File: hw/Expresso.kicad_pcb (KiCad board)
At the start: 4 copper layers, 76.2 x 59.4 mm, 93 parts, among them J1 USB_C_Receptacle_USB2.0_16P, J11 Exp Connector, J13 Exp Connector, J3 Midi Out, J5 Debug, J7 Exp Connector, J9 Exp Connector, SW1 Reset, SW2 Boot0, U1 XC6206P332MR, U10 NE5532, U2 XC6206P332MR, U3 STM32G431CBT6, U4 SRV05-4, U5 74HC14, U7 NE5532, U8 NE5532, U9 NE5532, Y1 16 MHz

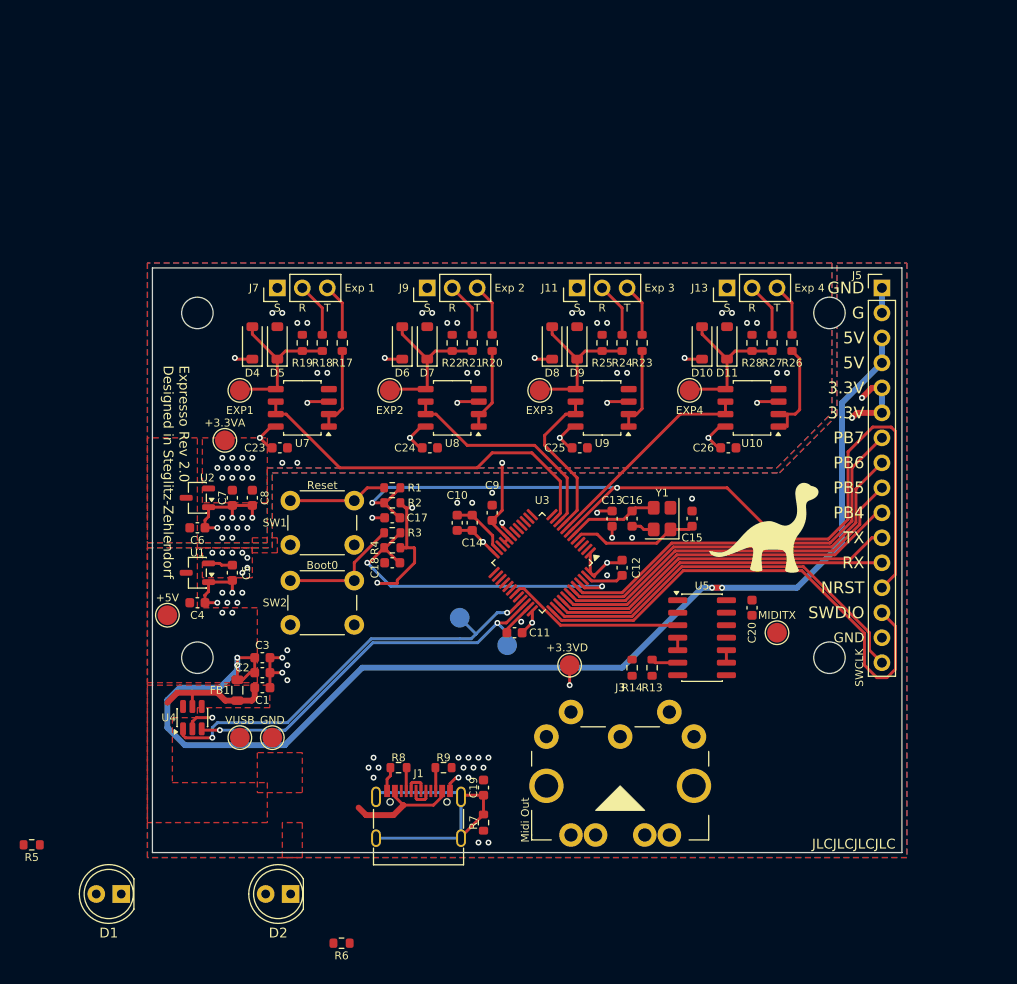
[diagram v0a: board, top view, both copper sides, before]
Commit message: added new pcb design, ERC errors not fixed yet
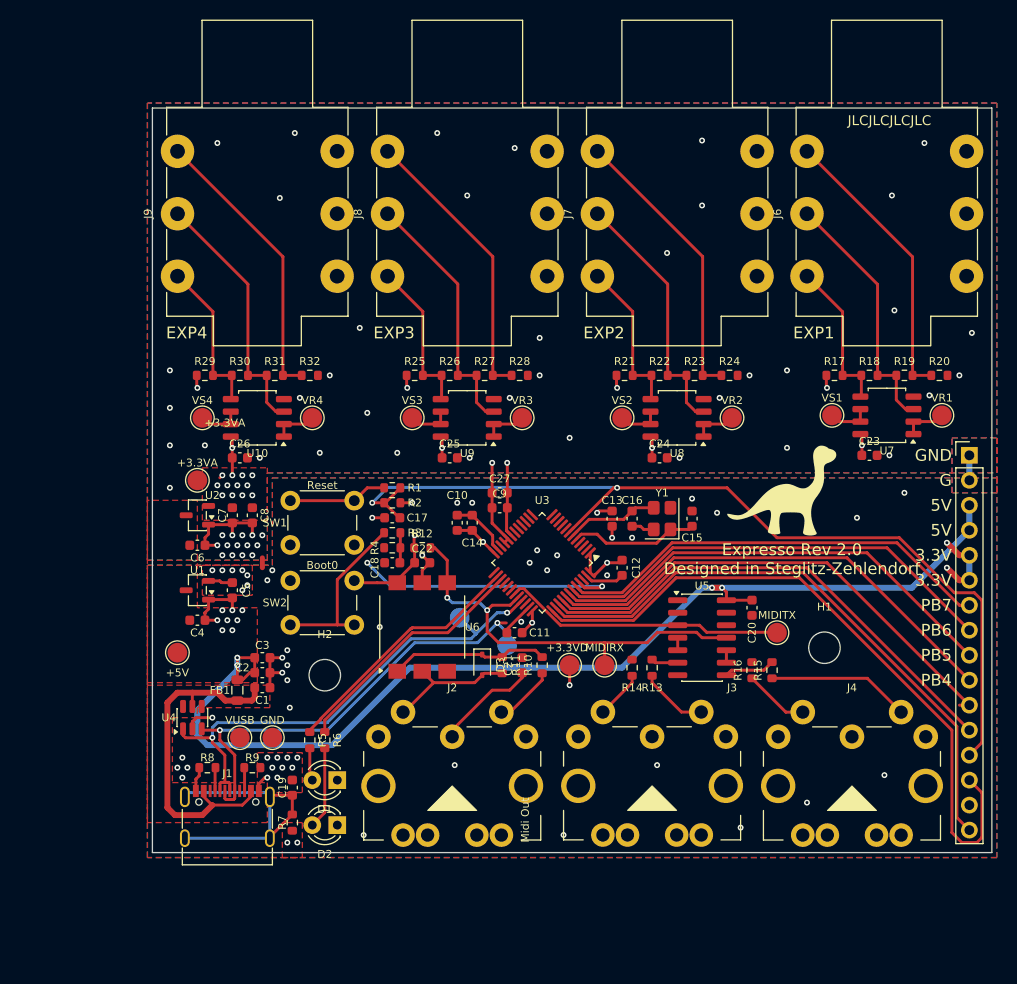
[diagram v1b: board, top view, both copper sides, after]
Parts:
- removed D10, D11, D4, D5, D6, D7, D8, D9: B5819W SL, Diode_SMD:D_SOD-123
- removed H3, H4: MountingHole, MountingHole:MountingHole_3.2mm_M3
- removed J11, J13: Exp Connector, Connector_PinHeader_2.54mm:PinHeader_1x03_P2.54mm_Vertical
- added C21: 100n, Capacitor_SMD:C_0603_1608Metric, F.Cu at (161.0, 126.2)
- added C22: 100n, Capacitor_SMD:C_0603_1608Metric, F.Cu at (150.9, 115.8)
- added C27: 1u, Capacitor_SMD:C_0603_1608Metric, F.Cu at (158.8, 108.7)
- added D3: 1N4148WS, Diode_SMD:D_SOD-323, F.Cu at (157.0, 126.2)
- added J2: Midi In, DIN5_MIDI_MultiGround:DIN5_MIDI_MultiGround, F.Cu at (153.9, 133.5)
- added J4: Midi Thru, DIN5_MIDI_MultiGround:DIN5_MIDI_MultiGround, F.Cu at (194.6, 133.5)
- added J6: Exp, Connector_Audio:Jack_6.35mm_Neutrik_NMJ6HFD4_Horizontal, F.Cu at (190.0, 86.7)
- added J8: Exp, Connector_Audio:Jack_6.35mm_Neutrik_NMJ6HFD4_Horizontal, F.Cu at (147.3, 86.7)
- added NT1: GND_GNDA, NetTie:NetTie-2_SMD_Pad0.5mm, F.Cu at (134.6, 115.8)
- added R10: 220, Resistor_SMD:R_0603_1608Metric, F.Cu at (163.1, 126.2)
- added R11: 1k, Resistor_SMD:R_0603_1608Metric, F.Cu at (159.0, 126.2)
- added R12: 1k, Resistor_SMD:R_0603_1608Metric, F.Cu at (150.9, 114.3)
- added R15: 220, Resistor_SMD:R_0603_1608Metric, F.Cu at (186.4, 126.7)
- added R16: 220, Resistor_SMD:R_0603_1608Metric, F.Cu at (184.4, 126.7)
- added R29: 10k, Resistor_SMD:R_0603_1608Metric, F.Cu at (128.8, 96.8)
- added R30: 100k, Resistor_SMD:R_0603_1608Metric, F.Cu at (132.3, 96.8)
- added R31: 100k, Resistor_SMD:R_0603_1608Metric, F.Cu at (135.9, 96.8)
- added R32: 10k, Resistor_SMD:R_0603_1608Metric, F.Cu at (139.4, 96.8)
- added TP11: VS, TestPoint:TestPoint_Pad_D2.0mm, F.Cu at (192.5, 100.8)
- added TP13: VS, TestPoint:TestPoint_Pad_D2.0mm, F.Cu at (171.2, 101.1)
- added TP15: VS, TestPoint:TestPoint_Pad_D2.0mm, F.Cu at (149.9, 101.1)
- added TP17: VS, TestPoint:TestPoint_Pad_D2.0mm, F.Cu at (128.5, 101.1)
- added TP8: MIDI_RX, TestPoint:TestPoint_Pad_D2.0mm, F.Cu at (169.4, 126.2)
- added U6: H11L1, SOP-6-2.54mm:SOP-6_6.35x8.51mm_P02.54mm, F.Cu at (150.9, 122.4)
- D1, D2: footprint LED_THT:LED_D5.0mm -> LED_THT:LED_D3.0mm
- J7, J9: value Exp Connector -> Exp; footprint Connector_PinHeader_2.54mm:PinHeader_1x03_P2.54mm_Vertical -> Connector_Audio:Jack_6.35mm_Neutrik_NMJ6HFD4_Horizontal
- R17, R20, R21, R24: value 1k -> 10k
- R18, R23, R26, R27: value 1k -> 100k
- R19, R22: value 2M -> 100k
- R25, R28: value 2M -> 10k
- TP10: renamed from TP8; value EXP -> VR
- TP12: renamed from TP9; value EXP -> VR
- TP14: renamed from TP10; value EXP -> VR
- TP16: renamed from TP11; value EXP -> VR
- moved H1 72.3 mm to (191.8, 124.5)
- moved TP10 71.4 mm to (203.7, 100.8)
- moved H2 63.2 mm to (141.0, 127.3)
- moved R19 61.3 mm to (199.9, 96.8), turned to 0 degrees
- moved C23 59.9 mm to (196.3, 104.9)
- moved U7 59.4 mm to (198.1, 100.8)
- moved R18 55.7 mm to (196.3, 96.8), turned to 0 degrees
- moved U10 50.3 mm to (134.1, 101.1)
- moved R17 50.1 mm to (192.8, 96.8), turned to 0 degrees
- moved C26 49.7 mm to (132.3, 105.2)
- moved R20 45.6 mm to (203.5, 96.8), turned to 0 degrees
- moved TP16 38.5 mm to (139.7, 101.1)
- moved R26 35.0 mm to (153.7, 96.8), turned to 0 degrees
- moved TP12 34.9 mm to (182.4, 101.1)
- moved J7 32.6 mm to (168.7, 86.7)
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- renumbered TP13 to TP6, TP12 to TP7, TP7 to TP9
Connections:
- C23 pad 2: GND -> GNDA
- C24 pad 2: GND -> GNDA
- C25 pad 2: GND -> GNDA
- C26 pad 2: GND -> GNDA
- C6 pad 2: GND -> GNDA
- C7 pad 2: GND -> GNDA
- C8 pad 2: GND -> GNDA
- C9 pad 2: GND -> GNDA
- R17 pad 1: Net-(J7-Pin_3) -> +3.3VA
- R17 pad 2: /Expression Inputs/Expression Input 1/EXP_REF -> /Expression Inputs/Expression Input 1/EXP_T
- R18 pad 1: Net-(J7-Pin_2) -> /Expression Inputs/Expression Input 1/EXP_T
- R18 pad 2: /Expression Inputs/Expression Input 1/EXP_SENSE -> /Expression Inputs/Expression Input 1/EXP_R
- R19 pad 1: /Expression Inputs/Expression Input 1/EXP_SENSE -> /Expression Inputs/Expression Input 1/EXP_R
- R19 pad 2: GND -> /Expression Inputs/Expression Input 1/EXP_S
- R20 pad 1: Net-(J9-Pin_3) -> /Expression Inputs/Expression Input 1/EXP_S
- R20 pad 2: /Expression Inputs/Expression Input 2/EXP_REF -> GNDA
- R21 pad 1: Net-(J9-Pin_2) -> +3.3VA
- R21 pad 2: /Expression Inputs/Expression Input 2/EXP_SENSE -> /Expression Inputs/Expression Input 2/EXP_T
- R22 pad 1: /Expression Inputs/Expression Input 2/EXP_SENSE -> /Expression Inputs/Expression Input 2/EXP_T
- R22 pad 2: GND -> /Expression Inputs/Expression Input 2/EXP_R
- R23 pad 1: Net-(J11-Pin_3) -> /Expression Inputs/Expression Input 2/EXP_R
- R23 pad 2: /Expression Inputs/Expression Input 3/EXP_REF -> /Expression Inputs/Expression Input 2/EXP_S
- R24 pad 1: Net-(J11-Pin_2) -> /Expression Inputs/Expression Input 2/EXP_S
- R24 pad 2: /Expression Inputs/Expression Input 3/EXP_SENSE -> GNDA
- R25 pad 1: /Expression Inputs/Expression Input 3/EXP_SENSE -> +3.3VA
- R25 pad 2: GND -> /Expression Inputs/Expression Input 3/EXP_T
- R26 pad 1: Net-(J13-Pin_3) -> /Expression Inputs/Expression Input 3/EXP_T
- R26 pad 2: /Expression Inputs/Expression Input 4/EXP_REF -> /Expression Inputs/Expression Input 3/EXP_R
- R27 pad 1: Net-(J13-Pin_2) -> /Expression Inputs/Expression Input 3/EXP_R
- R27 pad 2: /Expression Inputs/Expression Input 4/EXP_SENSE -> /Expression Inputs/Expression Input 3/EXP_S
- R28 pad 1: /Expression Inputs/Expression Input 4/EXP_SENSE -> /Expression Inputs/Expression Input 3/EXP_S
- R28 pad 2: GND -> GNDA
- R4 pad 1: STM_BOOT0 -> GND
- R4 pad 2: +3.3V -> STM_BOOT0
- SW2 pad 1: GND -> Net-(R3-Pad1)
- SW2 pad 2: Net-(R3-Pad1) -> +3.3V
- TP10 pad 1: /Expression Inputs/Expression Input 1/EXP_SENSE -> /Expression Inputs/Expression Input 1/VR
- TP12 pad 1: /Expression Inputs/Expression Input 2/EXP_SENSE -> /Expression Inputs/Expression Input 2/VR
- TP14 pad 1: /Expression Inputs/Expression Input 3/EXP_SENSE -> /Expression Inputs/Expression Input 3/VR
- TP16 pad 1: /Expression Inputs/Expression Input 4/EXP_SENSE -> /Expression Inputs/Expression Input 4/VR
- U10 pad 1: /Expression Inputs/Expression Input 4/EXP_REF -> /Expression Inputs/Expression Input 4/VR
- U10 pad 2: /Expression Inputs/Expression Input 4/EXP_REF -> /Expression Inputs/Expression Input 4/VR
- U10 pad 3: +3.3VA -> /Expression Inputs/Expression Input 4/EXP_R
- U10 pad 4: GND -> GNDA
- U10 pad 5: /Expression Inputs/Expression Input 4/EXP_SENSE -> /Expression Inputs/Expression Input 4/EXP_T
- U10 pad 6: STM_ADC1_IN1 -> /Expression Inputs/Expression Input 4/VS
- U10 pad 7: STM_ADC1_IN1 -> /Expression Inputs/Expression Input 4/VS
- U2 pad 1: GND -> GNDA
- U3 pad 19: GND -> GNDA
- U3 pad 32: unconnected-(U3-PA10-Pad32) -> STM_USART1_RX
- U5 pad 1: GND -> (no net)
- U5 pad 10: unconnected-(U5-Pad10) -> Net-(U5-Pad10)
- U5 pad 11: GND -> STM_USART1_RX
- U5 pad 12: unconnected-(U5-Pad12) -> (no net)
- U5 pad 13: GND -> (no net)
- U5 pad 2: unconnected-(U5-Pad2) -> (no net)
- U5 pad 8: unconnected-(U5-Pad8) -> Net-(R15-Pad2)
- U5 pad 9: GND -> Net-(U5-Pad10)
- U7 pad 1: /Expression Inputs/Expression Input 1/EXP_REF -> /Expression Inputs/Expression Input 1/VR
- U7 pad 2: /Expression Inputs/Expression Input 1/EXP_REF -> /Expression Inputs/Expression Input 1/VR
- U7 pad 3: +3.3VA -> /Expression Inputs/Expression Input 1/EXP_R
- U7 pad 4: GND -> GNDA
- U7 pad 5: /Expression Inputs/Expression Input 1/EXP_SENSE -> /Expression Inputs/Expression Input 1/EXP_T
- U7 pad 6: STM_ADC1_IN4 -> /Expression Inputs/Expression Input 1/VS
- U7 pad 7: STM_ADC1_IN4 -> /Expression Inputs/Expression Input 1/VS
- U8 pad 1: /Expression Inputs/Expression Input 2/EXP_REF -> /Expression Inputs/Expression Input 2/VR
- U8 pad 2: /Expression Inputs/Expression Input 2/EXP_REF -> /Expression Inputs/Expression Input 2/VR
- U8 pad 3: +3.3VA -> /Expression Inputs/Expression Input 2/EXP_R
- U8 pad 4: GND -> GNDA
- U8 pad 5: /Expression Inputs/Expression Input 2/EXP_SENSE -> /Expression Inputs/Expression Input 2/EXP_T
- U8 pad 6: STM_ADC1_IN3 -> /Expression Inputs/Expression Input 2/VS
- U8 pad 7: STM_ADC1_IN3 -> /Expression Inputs/Expression Input 2/VS
- U9 pad 1: /Expression Inputs/Expression Input 3/EXP_REF -> /Expression Inputs/Expression Input 3/VR
- U9 pad 2: /Expression Inputs/Expression Input 3/EXP_REF -> /Expression Inputs/Expression Input 3/VR
- U9 pad 3: +3.3VA -> /Expression Inputs/Expression Input 3/EXP_R
- U9 pad 4: GND -> GNDA
- U9 pad 5: /Expression Inputs/Expression Input 3/EXP_SENSE -> /Expression Inputs/Expression Input 3/EXP_T
- U9 pad 6: STM_ADC1_IN2 -> /Expression Inputs/Expression Input 3/VS
- U9 pad 7: STM_ADC1_IN2 -> /Expression Inputs/Expression Input 3/VS
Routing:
- net STM_USART1_RX: track 0.00 -> 44.3 mm, vias 0 -> 2
- net STM_ADC1_IN4: track 38.2 -> 0.00 mm
- net /Expression Inputs/Expression Input 1/EXP_S: track 0.00 -> 29.1 mm
- net /Expression Inputs/Expression Input 4/EXP_S: track 0.00 -> 29.1 mm
- net /Expression Inputs/Expression Input 2/EXP_S: track 0.00 -> 29.1 mm
- net /Expression Inputs/Expression Input 3/EXP_S: track 0.00 -> 29.1 mm
- net /Expression Inputs/Expression Input 2/EXP_R: track 0.00 -> 26.5 mm
- net /Expression Inputs/Expression Input 4/EXP_R: track 0.00 -> 26.2 mm
- net /Expression Inputs/Expression Input 3/EXP_R: track 0.00 -> 26.2 mm
- net /Expression Inputs/Expression Input 1/EXP_R: track 0.00 -> 25.9 mm
- net STM_LED1: track 0.00 -> 25.8 mm
- net STM_LED2: track 0.00 -> 25.0 mm
- net STM_ADC1_IN3: track 23.1 -> 0.00 mm
- net STM_ADC1_IN1: track 22.3 -> 0.00 mm
- net STM_SWCLK: track 40.7 -> 60.6 mm
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- added copper zone on B.Cu, net GNDA
- added copper zone on F.Cu, net GNDA
- added copper zone on In1.Cu, net GNDA
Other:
- board size 76.2 x 59.4 mm -> 85.3 x 75.7 mm
- board text added: "MIDIRX"
- board text added: "VR1"
- board text added: "VR2"
- board text added: "VR3"
- board text added: "VR4"
- board text added: "VS1"
- board text added: "VS2"
- board text added: "VS3"
- board text added: "VS4"
- board text removed: "Exp 1"
- board text removed: "Exp 2"
- board text removed: "Exp 3"
- board text removed: "Exp 4"
- board text removed: "R"
- board text removed: "S"
- board text removed: "T"

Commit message: small PCB updates for casing design
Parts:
- added H3: MountingHole, MountingHole:MountingHole_3.2mm_M3, F.Cu at (144.8, 98.8)
- added H4: MountingHole, MountingHole:MountingHole_3.2mm_M3, F.Cu at (187.5, 98.8)
- moved J2 1.01 mm to (153.9, 132.5)
- moved J3 1.01 mm to (174.2, 132.5)
- moved J4 1.01 mm to (194.6, 132.5)
- moved C20 0.51 mm to (184.4, 119.9)
- moved R15 0.51 mm to (186.4, 126.2)
- moved R16 0.51 mm to (184.4, 126.2)
- moved U5 0.51 mm to (179.3, 122.9)
- moved TP3 0.25 mm to (165.9, 126.0)
- moved TP8 0.25 mm to (169.4, 126.0)
- moved U6 0.25 mm to (150.9, 122.1)
- moved C21 0.22 mm to (161.0, 126.0)
- moved D3 0.22 mm to (157.0, 126.0)
- moved R10 0.22 mm to (163.1, 126.0)
- moved R11 0.22 mm to (159.0, 126.0)
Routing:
- net +3.3V: track 37.7 -> 30.5 mm
- net STM_USART1_RX: track 44.3 -> 38.2 mm
- net STM_USB_DP: track 47.5 -> 50.2 mm
- net GND: track 44.7 -> 42.3 mm
- net +5V: track 112.7 -> 110.5 mm
- net GNDA: track 17.9 -> 19.3 mm, vias 53 -> 54
- net +3.3VA: track 25.9 -> 27.1 mm, vias 21 -> 22
- net Net-(C21-Pad1): track 10.5 -> 9.48 mm
- net Net-(J3-Pad5): track 4.91 -> 4.08 mm
- net Net-(J3-Pad4): track 6.94 -> 6.11 mm
- net Net-(J2-Pad4): track 6.19 -> 5.45 mm

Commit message: updates to hardware layer
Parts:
- added C28: 100n, Capacitor_SMD:C_0603_1608Metric, F.Cu at (142.5, 133.9)
- moved TP9 0.76 mm to (186.9, 122.2)
- moved R13 0.51 mm to (174.2, 126.0)
- moved R14 0.51 mm to (172.2, 126.0)
- moved TP1 0.51 mm to (132.3, 133.1)
- moved TP5 0.51 mm to (135.6, 133.1)
- moved C24 0.25 mm to (175.0, 104.9)
- moved C25 0.25 mm to (153.7, 104.9)
- moved R15 0.25 mm to (186.4, 126.0)
- moved R16 0.25 mm to (184.4, 126.0)
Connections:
- TP10 pad 1: /Expression Inputs/Expression Input 1/VR -> STM_ADC1_IN1
- TP11 pad 1: /Expression Inputs/Expression Input 1/VS -> STM_ADC1_IN2
- TP12 pad 1: /Expression Inputs/Expression Input 2/VR -> STM_ADC1_IN3
- TP13 pad 1: /Expression Inputs/Expression Input 2/VS -> STM_ADC1_IN4
- TP14 pad 1: /Expression Inputs/Expression Input 3/VR -> STM_ADC2_IN17
- TP15 pad 1: /Expression Inputs/Expression Input 3/VS -> STM_ADC2_IN13
- TP16 pad 1: /Expression Inputs/Expression Input 4/VR -> STM_ADC2_IN3
- TP17 pad 1: /Expression Inputs/Expression Input 4/VS -> STM_ADC2_IN4
- U10 pad 1: /Expression Inputs/Expression Input 4/VR -> STM_ADC2_IN3
- U10 pad 2: /Expression Inputs/Expression Input 4/VR -> STM_ADC2_IN3
- U10 pad 6: /Expression Inputs/Expression Input 4/VS -> STM_ADC2_IN4
- U10 pad 7: /Expression Inputs/Expression Input 4/VS -> STM_ADC2_IN4
- U3 pad 12: unconnected-(U3-PA4-Pad12) -> STM_ADC2_IN17
- U3 pad 13: unconnected-(U3-PA5-Pad13) -> STM_ADC2_IN13
- U3 pad 14: unconnected-(U3-PA6-Pad14) -> STM_ADC2_IN3
- U3 pad 15: unconnected-(U3-PA7-Pad15) -> STM_ADC2_IN4
- U5 pad 1: (no net) -> GND
- U5 pad 12: (no net) -> unconnected-(U5-Pad12)
- U5 pad 13: (no net) -> GND
- U5 pad 2: (no net) -> unconnected-(U5-Pad2)
- U7 pad 1: /Expression Inputs/Expression Input 1/VR -> STM_ADC1_IN1
- U7 pad 2: /Expression Inputs/Expression Input 1/VR -> STM_ADC1_IN1
- U7 pad 6: /Expression Inputs/Expression Input 1/VS -> STM_ADC1_IN2
- U7 pad 7: /Expression Inputs/Expression Input 1/VS -> STM_ADC1_IN2
- U8 pad 1: /Expression Inputs/Expression Input 2/VR -> STM_ADC1_IN3
- U8 pad 2: /Expression Inputs/Expression Input 2/VR -> STM_ADC1_IN3
- U8 pad 6: /Expression Inputs/Expression Input 2/VS -> STM_ADC1_IN4
- U8 pad 7: /Expression Inputs/Expression Input 2/VS -> STM_ADC1_IN4
- U9 pad 1: /Expression Inputs/Expression Input 3/VR -> STM_ADC2_IN17
- U9 pad 2: /Expression Inputs/Expression Input 3/VR -> STM_ADC2_IN17
- U9 pad 6: /Expression Inputs/Expression Input 3/VS -> STM_ADC2_IN13
- U9 pad 7: /Expression Inputs/Expression Input 3/VS -> STM_ADC2_IN13
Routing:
- net STM_ADC1_IN1: track 0.00 -> 44.5 mm
- net STM_ADC2_IN4: track 0.00 -> 41.0 mm
- net STM_ADC1_IN2: track 0.00 -> 38.2 mm
- net STM_ADC2_IN3: track 0.00 -> 35.4 mm
- net STM_ADC1_IN3: track 0.00 -> 23.4 mm
- net STM_ADC2_IN13: track 0.00 -> 20.2 mm
- net GND: track 42.3 -> 61.5 mm, vias 56 -> 68
- net STM_ADC1_IN4: track 0.00 -> 17.3 mm
- net STM_ADC2_IN17: track 0.00 -> 15.5 mm
- net /Midi Connector/MIDI_IN_SHIELD: track 0.00 -> 14.9 mm
- net STM_NRST: track 95.9 -> 83.1 mm
- net STM_USART1_RX: track 38.2 -> 44.0 mm
- net /Expression Inputs/Expression Input 4/VS: track 4.42 -> 0.00 mm
- net /Expression Inputs/Expression Input 2/VS: track 4.42 -> 0.00 mm
- net /Expression Inputs/Expression Input 3/VR: track 4.42 -> 0.00 mm
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- added copper zone on B.Cu, net /Midi Connector/MIDI_IN_SHIELD
- added copper zone on F.Cu, net /Midi Connector/MIDI_IN_SHIELD
- added copper zone on In1.Cu, net /Midi Connector/MIDI_IN_SHIELD
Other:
- board text added: "CLK"
- board text added: "DIO"
- board text added: "Expresso Rev 2.0 Designed in Steglitz-Zehlendorf by Amon Benson"
- board text added: "MIDI In"
- board text added: "MIDI Out"
- board text added: "MIDI Thru"
- board text added: "RST"
- board text removed: "Expresso Rev 2.0 Designed in Steglitz-Zehlendorf"
- board text removed: "G"
- board text removed: "Midi Out"
- board text removed: "NRST"
- board text removed: "SWCLK"
- board text removed: "SWDIO"
